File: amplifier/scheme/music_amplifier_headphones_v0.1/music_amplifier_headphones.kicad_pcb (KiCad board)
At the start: 2 copper layers, 55 x 55 mm, 31 parts, among them J1 Power, J2 Input, J3 Indicator, J4 Output, SW1 Power

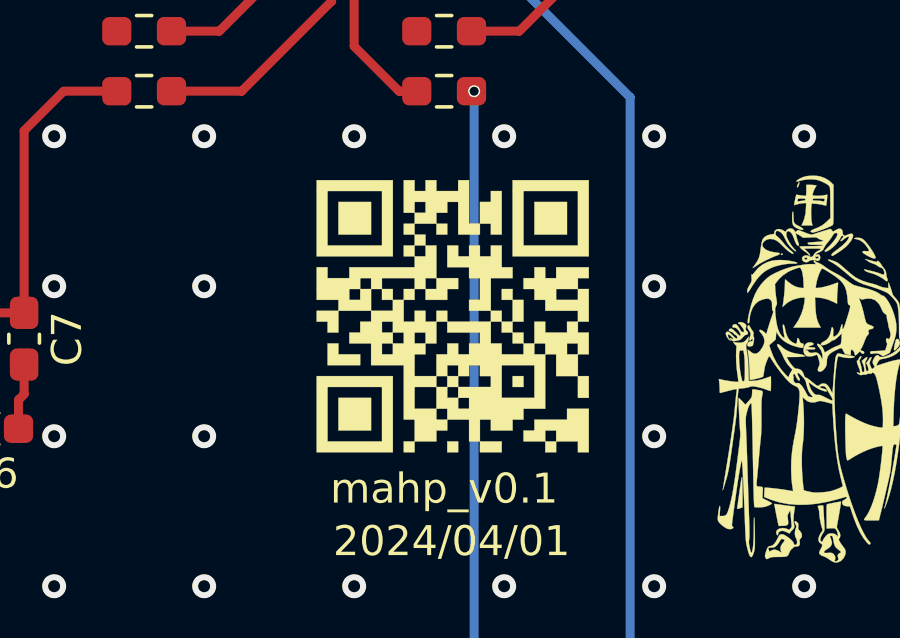
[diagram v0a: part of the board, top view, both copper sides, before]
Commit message: small: QR code
Change QR code from github to site.
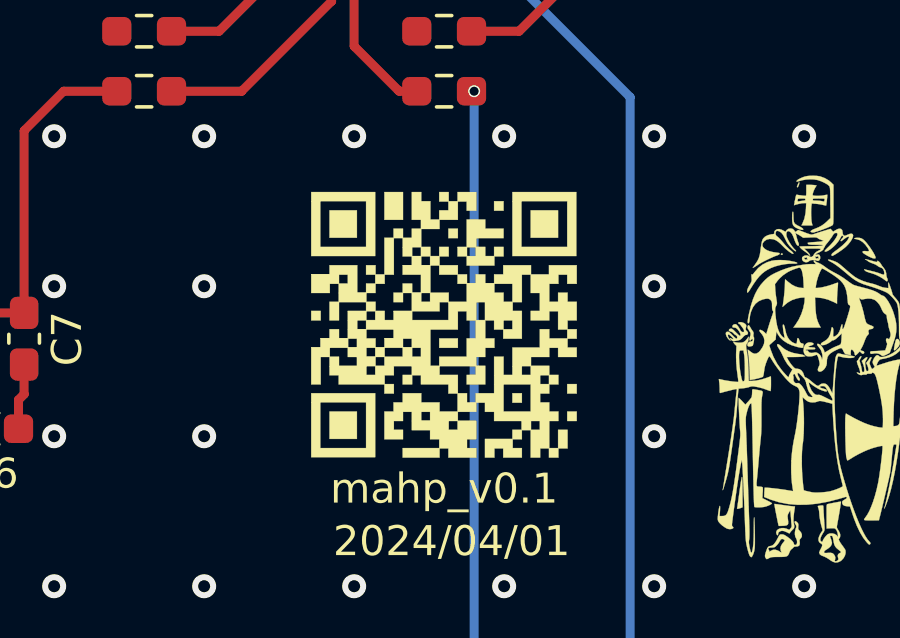
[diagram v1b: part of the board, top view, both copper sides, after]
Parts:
- removed the G*** at (158.2, 81.0)
- added G***: LOGO, mine:qr_code, F.Cu at (158.0, 81.3)
